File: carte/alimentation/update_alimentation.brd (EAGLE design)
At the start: 160 x 100 mm, 81 parts, among them IC1 LM2596T, IC2 LM2596T, IC4 DSPIC33FJ128MC804PT, J4 RJ11-2L-B, K2 RP811005, U2 LP2985-33DBVR, X10 22-23-2021, X11 22-23-2021, X9 22-23-2021

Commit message: LM2678S_ADJ dimmensionnement
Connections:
- removed net N$25 (its old number): C22.2
- removed net N$29: C20.1, C20.2
- new net N$24: C16.1
- net GND: now also C18.2, C21.2, D3.A, LM2678T-12.4; no longer C16.1
- net N$21: now also C16.2, C22.2; no longer C21.2
- net N$26: now also C19.2, C20.2; no longer C16.2, C18.2, D3.A, LM2678T-12.4
- net N$28: now also C20.1; no longer C19.2
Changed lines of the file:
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@@
 <?xml version="1.0" encoding="utf-8"?>
 <!DOCTYPE eagle SYSTEM "eagle.dtd">
-<eagle version="8.7.0">
+<eagle version="9.0.0">
 <drawing>
 <settings>
@@
 <contactref element="J3" pad="4"/>
 <contactref element="D2" pad="A"/>
-<contactref element="C5" pad="2"/>
 <contactref element="C2" pad="2"/>
 <contactref element="C6" pad="1"/>
@@
 <contactref element="PAD13" pad="1"/>
 <contactref element="PAD14" pad="1"/>
-<contactref element="C16" pad="1"/>
+<contactref element="LM2678T-12" pad="4"/>
+<contactref element="C5" pad="2"/>
 <contactref element="LM2678T-12" pad="2"/>
-<wire x1="-99.91" y1="-3.81" x2="-120.65" y2="-27.155" width="0" layer="19" extent="1-1"/>
-<wire x1="-84.54" y1="7.62" x2="-99.91" y2="-3.81" width="0" layer="19" extent="1-1"/>
-<wire x1="-79.54" y1="1.82" x2="-84.54" y2="7.62" width="0" layer="19" extent="1-1"/>
+<contactref element="D3" pad="A"/>
+<contactref element="C21" pad="2"/>
+<contactref element="C18" pad="2"/>
+<wire x1="-108.37" y1="-34.29" x2="-118.53" y2="-58.42" width="0" layer="19" extent="1-1"/>
+<wire x1="-118.11" y1="-27.155" x2="-108.37" y2="-34.29" width="0" layer="19" extent="1-1"/>
+<wire x1="-120.65" y1="-27.155" x2="-118.11" y2="-27.155" width="0" layer="19" extent="1-1"/>
+<wire x1="-76.2" y1="-16.51" x2="-108.37" y2="-34.29" width="0" layer="19" extent="1-1"/>
+<wire x1="-79.54" y1="1.82" x2="-76.2" y2="-16.51" width="0" layer="19" extent="1-1"/>
+<wire x1="-84.54" y1="7.62" x2="-79.54" y2="1.82" width="0" layer="19" extent="1-1"/>
 <wire x1="-78.74" y1="13.42" x2="-84.54" y2="7.62" width="0" layer="19" extent="1-1"/>
 <wire x1="-72.94" y1="8.42" x2="-78.74" y2="13.42" width="0" layer="19" extent="1-1"/>
@@
 <contactref element="C21" pad="1"/>
 </signal>
-<signal name="N$21">
-<contactref element="C21" pad="2"/>
-</signal>
 <signal name="N$23">
 <contactref element="IC2" pad="3"/>
@@
 <wire x1="-65.1764" y1="24.13" x2="-68.58" y2="24.13" width="0" layer="19" extent="1-1"/>
 </signal>
-<signal name="N$24">
-<contactref element="C22" pad="1"/>
-</signal>
-<signal name="N$26">
-<contactref element="D3" pad="A"/>
-<contactref element="C18" pad="2"/>
-<contactref element="LM2678T-12" pad="4"/>
-<contactref element="C16" pad="2"/>
-<wire x1="-108.37" y1="-34.29" x2="-118.11" y2="-27.155" width="0" layer="19" extent="1-1"/>
-<wire x1="-98.21" y1="-3.81" x2="-118.11" y2="-27.155" width="0" layer="19" extent="1-1"/>
-<wire x1="-76.2" y1="-16.51" x2="-98.21" y2="-3.81" width="0" layer="19" extent="1-1"/>
-</signal>
-<signal name="N$25">
-<contactref element="C22" pad="2"/>
-</signal>
 <signal name="N$27">
 <contactref element="IC1" pad="3"/>
@@
 <contactref element="L4" pad="2"/>
 </signal>
+<signal name="N$21">
+<contactref element="C22" pad="2"/>
+<contactref element="C16" pad="2"/>
+<wire x1="-98.21" y1="-3.81" x2="-118.53" y2="-62.23" width="0" layer="19" extent="1-1"/>
+</signal>
+<signal name="N$26">
+<contactref element="C19" pad="2"/>
+<contactref element="C20" pad="2"/>
+<wire x1="-118.53" y1="-66.04" x2="-118.53" y2="-69.85" width="0" layer="19" extent="1-1"/>
+</signal>
 <signal name="N$22">
+<contactref element="C22" pad="1"/>
+</signal>
+<signal name="N$24">
+<contactref element="C16" pad="1"/>
+</signal>
+<signal name="N$25">
 <contactref element="C19" pad="1"/>
 </signal>
 <signal name="N$28">
-<contactref element="C19" pad="2"/>
-</signal>
-<signal name="N$29">
-<contactref element="C20" pad="2"/>
 <contactref element="C20" pad="1"/>
-<wire x1="-118.53" y1="-69.85" x2="-120.23" y2="-69.85" width="0" layer="19" extent="1-1"/>
 </signal>
 </signals>

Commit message: carte alim maj sch/brd
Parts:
- removed C3: 1000u, resistor:C0603
- removed D1, D2, D3: 1N5624, diode:DO201-15
- removed K2: RP811005, relay:RT-C/O12A5
- removed L1, L2: (no value), inductor-neosid:SM-L15A
- removed L4: 15uH, inductor-coilcraft:DO3316P
- removed LED2: (no value), eagle-ltspice:LED_1206
- added C23, C24, C25: 100uF, rcl:C1210
- added C26, C30: 10uF, rcl:D/7343-31W
- added C27: 220uF, rcl:D/7343-31W
- added C28, C29: 68uF, rcl:D/7343-31W
- added LED1: RED, led:LED5MM
- added LM2678S_ADJ: (no value), Robot_MT:TO-220-7
- added R7: 4.12k, resistor:R0805
- added R8: 1k, resistor:R0805
- added U$10, U$11: 53uH, Robot_MT:KM-3.0_5V3A
- added U$12: RJ26FX102, Robot_MT:RJ6S
- added U$2, U$3: (no value), Robot_MT:TO220ACS
- added U$4, U$5: (no value), Robot_MT:DO-201AD
- added U$6: T9GV1L14-5, Robot_MT:T9G
- added U$7: BSH108, Robot_MT:SOT23
- added U$8: 22.8uH, Robot_MT:KM-3.0
- added U$9: 14.8uH, Robot_MT:KM-2.1
- C1: value (none) -> 220uF; device resistor:C0603 -> rcl:D/7343-31W
- C16, C19, C20: device resistor:C0603 -> rcl:D/7343-31W
- C17: device resistor:C0603 -> rcl:C0603
- C18, C21: value 180uF -> 68uF; device resistor:C0603 -> rcl:D/7343-31W
- C2, C4: value (none) -> 330uF; device resistor:C0603 -> rcl:D/7343-31W
- C22: value 10uF -> 0.01uF; device resistor:C0603 -> rcl:C0603
- C5: value (none) -> 1000uF; device resistor:C0603 -> rcl:E7,5-16
- R5: value 220 -> 500
- moved X9 245.8 mm to (156.5, 85.1), turned to 90 degrees
- moved C17 240.8 mm to (123.2, 62.2)
- moved C22 237.0 mm to (71.1, 78.7), turned to 90 degrees
- moved LM2678T-12 233.4 mm to (89.3, 96.9)
- moved C13 227.4 mm to (146.1, 77.5)
- moved X12 227.2 mm to (156.0, 65.5), turned to 270 degrees
- moved PAD13 223.8 mm to (142.2, 83.8)
- moved C12 221.3 mm to (143.5, 69.8)
- moved X1 215.9 mm to (156.0, 51.9), turned to 270 degrees
- moved PAD11 214.9 mm to (146.1, 83.8)
- moved PAD6 214.9 mm to (133.3, 88.9)
- moved PAD5 213.6 mm to (138.4, 88.9)
- moved PAD4 211.1 mm to (142.2, 88.9)
- moved C11 208.7 mm to (134.6, 69.8)
- moved Q1 208.6 mm to (141.0, 55.9), turned to 180 degrees
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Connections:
- removed net N$14 (its old number): C18.1, LM2678T-12.6
- removed net N$20: C21.1
- removed net N$21: C16.2, C22.2
- removed net N$22: C22.1
- removed net N$23: IC2.3, IC2.5
- removed net N$24: C16.1
- removed net N$25: C19.1
- removed net N$26: C19.2, C20.2
- removed net N$27: IC1.3, IC1.5
- removed net N$28: C20.1
- removed net RB0: D5.A, K2.A2
- removed net RB1: LED2.C, R5.1
- new net 5V_3A: X10.1, X11.1, X12.2, X9.1
- new net N$15: C16.+, C19.+, C20.+, C26.+, C30.+, C4.+, C5.+, IC2.1, LM2678S_ADJ.2, LM2678T-12.2, R8.1, U$6.K, X1.1
- new net RA7: IC4.13, LED1.K, U$7.1
- new net RA8: IC4.32, R5.1
- new net V+: C18.+, C21.+, C28.+, C29.+, U$9.2
- net +5V: now also C1.+, D5.C, U$11.2, U$6.B1; no longer C2.1, L2.2
- net +5V_3A: now also C27.+, U$10.2; no longer C1.1, L1.2
- net GND: now also C1.-, C16.-, C18.-, C19.-, C2.-, C20.-, C21.-, C23.2, C24.2, C25.2, C26.-, C27.-, C28.-, C29.-, C30.-, C4.-, C5.-, IC1.3, IC1.5, IC2.3, IC2.5, LM2678S_ADJ.4, U$2.A, U$3.A, U$4.A, U$5.A, U$7.2, X15.2; no longer C1.2, C18.2, C2.2, C21.2, C3.1, C5.2, D1.A, D2.A, D3.A, LM2678T-12.2
- net N$1: now also LED1.A, R5.2; no longer X13.1
- net N$11: now also C17.2, LM2678T-12.1, U$3.C, U$9.1; no longer C4.1, IC1.1, X15.2
- net N$12: now also U$10.1, U$4.C; no longer D1.C, L1.1
- net N$13: now also C22.1, LM2678S_ADJ.3; no longer C3.2, C5.1, IC2.1, K2.12, X1.1
- net N$16: now also C22.2, LM2678S_ADJ.1, U$2.C, U$8.1; no longer D5.C, K2.A1
- net N$17: now also C23.1, C24.1, C25.1, U$12.E, U$8.2; no longer C17.2, D3.C, LM2678T-12.1
- net N$18: now also D5.A, U$6.B2, U$7.3; no longer L4.1
- net N$19: now also R7.2, U$12.S; no longer L4.2
- net N$6: now also C2.+, IC1.1, U$6.A, X13.1; no longer C4.2, K2.11
- net N$7: now also LM2678S_ADJ.6, R7.1, R8.2; no longer LED2.A, R5.2
- net N$9: now also U$11.1, U$5.C; no longer D2.C, L2.1

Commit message: MAJ carte alim sch/brd
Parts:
- added R10, R11: 560, resistor:R0805
- added R12: 300, resistor:R0805
- added R13: 820, resistor:R0805
- added R14: 240, resistor:R0805
- added R15, R16: 200, resistor:R0805
- added R17: 1600, resistor:R0805
- added R18: 1100, resistor:R0805
- added R19: 220, resistor:R0805
- added R20: 1300, resistor:R0805
- added R9: 270, resistor:R0805
- moved LED1 104.6 mm to (91.4, 34.3)
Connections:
- net N$6 renamed BAT3+
- removed net N$3: X13.2, X14.1
- removed net N$4: X14.2, X15.1
- new net BAT12_11.1V: J2.4, J3.1, R13.1, X14.2, X15.1
- new net BAT1_3.7V: J3.3, R9.1
- new net BAT1_7.4V: J3.2, R11.1
- new net BAT23_22.2V: J1.4, J2.1, R17.1, X13.2, X14.1
- new net BAT2_14.8V: J2.3, R18.1
- new net BAT2_18.5V: J2.2, R20.1
- new net BAT3_25.9V: J1.3
- new net BAT3_29.6V: J1.2
- new net BAT3_33.3V: J1.1
- new net N$20: R10.2, R9.2
- new net N$21: R11.2, R12.2
- new net N$22: R13.2, R14.2
- new net N$23: R18.2, R19.2
- new net N$24: R15.2, R20.2
- new net N$25: R16.2, R17.2
- net GND: now also R10.1, R12.1, R14.1, R15.1, R16.1, R19.1; no longer J1.4, J2.4
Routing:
- net BAT3+: track 0.00 -> 12.7 mm

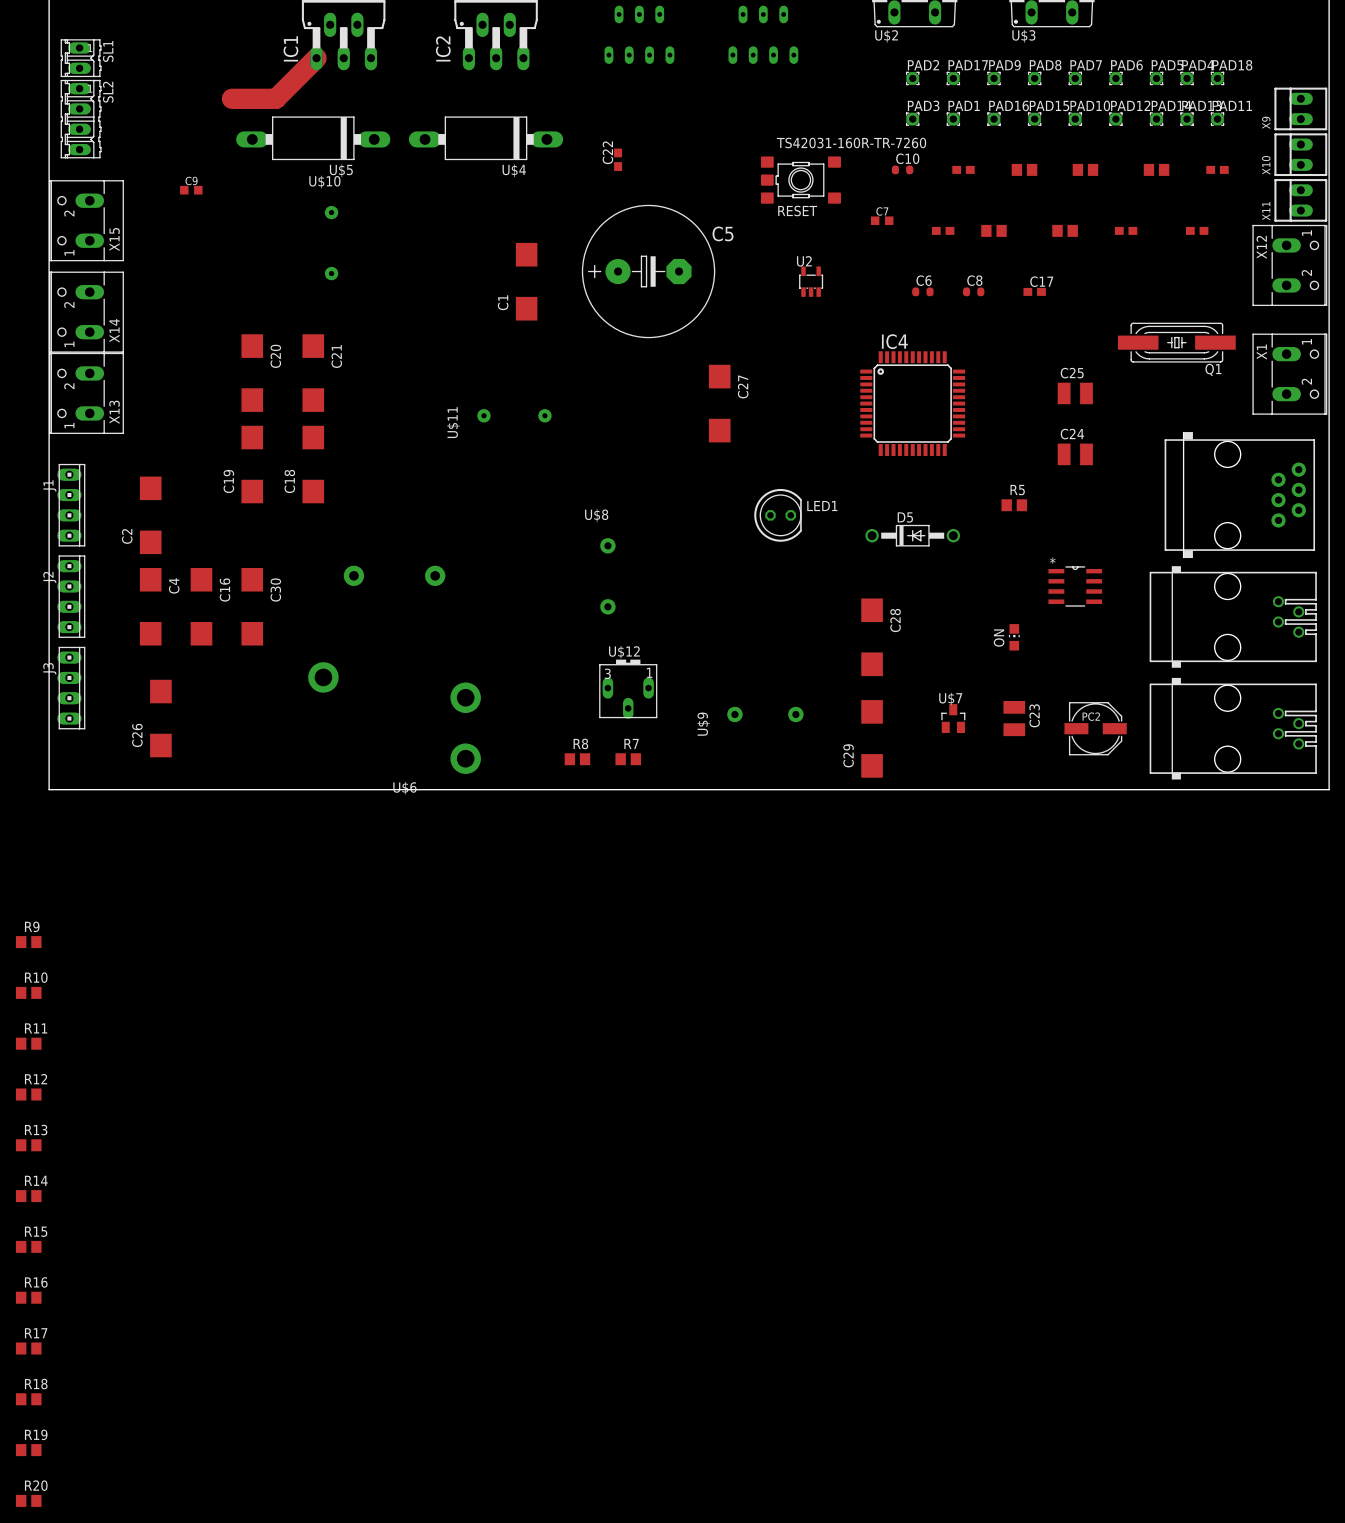
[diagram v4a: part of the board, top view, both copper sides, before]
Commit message: MAJ ancienne carte alim
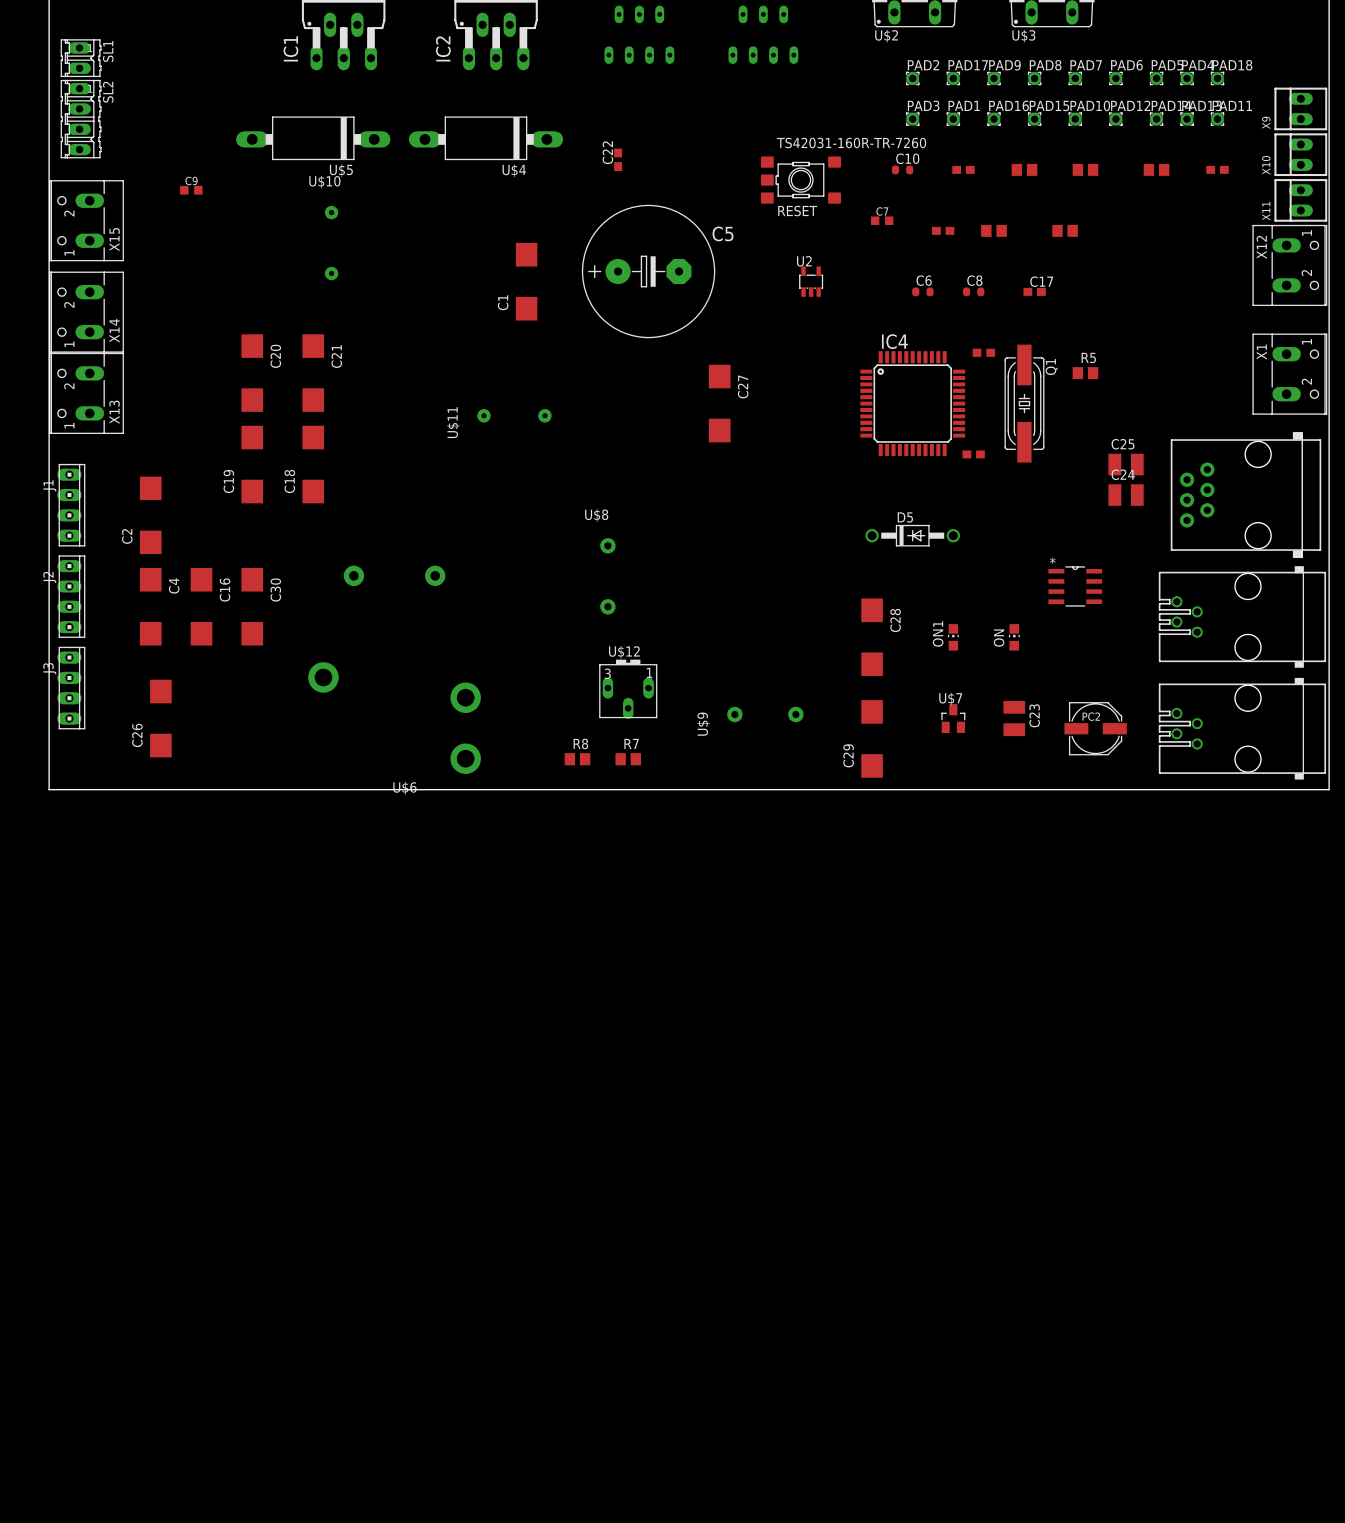
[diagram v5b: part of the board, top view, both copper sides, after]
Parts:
- removed LED1: RED, led:LED5MM
- removed R10, R11: 560, resistor:R0805
- removed R12: 300, resistor:R0805
- removed R13: 820, resistor:R0805
- removed R14: 240, resistor:R0805
- removed R15, R16: 200, resistor:R0805
- removed R17: 1600, resistor:R0805
- removed R18: 1100, resistor:R0805
- removed R19: 220, resistor:R0805
- removed R20: 1300, resistor:R0805
- removed R9: 270, resistor:R0805
- added ON1: GREEN, led:CHIP-LED0805
- moved C12 39.5 mm to (115.6, 41.9)
- moved C11 23.4 mm to (116.8, 54.6)
- moved Q1 20.5 mm to (121.9, 48.3), turned to 270 degrees
- moved R5 18.8 mm to (129.5, 52.1)
- moved C25 10.9 mm to (134.6, 40.6)
- moved C24 8.13 mm to (134.6, 36.8)
- moved J4 3.81 mm to (151.1, 36.8), turned to 90 degrees
- moved J5 2.54 mm to (149.9, 7.62), turned to 90 degrees
- moved J6 2.54 mm to (149.9, 21.6), turned to 90 degrees
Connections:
- net BAT3+ renamed N$6
- removed net BAT12_11.1V: J2.4, J3.1, R13.1, X14.2, X15.1
- removed net BAT1_3.7V: J3.3, R9.1
- removed net BAT1_7.4V: J3.2, R11.1
- removed net BAT23_22.2V: J1.4, J2.1, R17.1, X13.2, X14.1
- removed net BAT2_14.8V: J2.3, R18.1
- removed net BAT2_18.5V: J2.2, R20.1
- removed net BAT3_25.9V: J1.3
- removed net BAT3_29.6V: J1.2
- removed net BAT3_33.3V: J1.1
- removed net N$20: R10.2, R9.2
- removed net N$21: R11.2, R12.2
- removed net N$22: R13.2, R14.2
- removed net N$23: R18.2, R19.2
- removed net N$24: R15.2, R20.2
- removed net N$25: R16.2, R17.2
- new net N$3: X13.2, X14.1
- new net N$4: X14.2, X15.1
- net GND: now also J1.4, J2.4; no longer R10.1, R12.1, R14.1, R15.1, R16.1, R19.1
- net N$1: now also ON1.A; no longer LED1.A
- net RA7: now also ON1.C; no longer LED1.K
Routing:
- net N$6: track 12.7 -> 0.00 mm

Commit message: Modif board + ajout excel
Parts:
- moved U$10 57.2 mm to (36.6, 11.2), turned to 90 degrees
- moved C12 39.5 mm to (143.5, 69.8)
- moved U$11 36.7 mm to (49.3, 11.2)
- moved R7 33.3 mm to (94.0, 29.2)
- moved R8 30.7 mm to (81.3, 30.5)
- moved U$6 30.0 mm to (61.0, 40.6)
- moved C11 23.4 mm to (134.6, 69.8)
- moved Q1 20.5 mm to (141.0, 55.9), turned to 180 degrees
- moved U$12 19.1 mm to (91.4, 14.0)
- moved R5 18.8 mm to (120.7, 35.6)
- moved U$8 17.6 mm to (61.6, 11.2), turned to 90 degrees
- moved U$9 15.6 mm to (74.0, 11.0)
- moved C25 10.9 mm to (128.3, 49.5)
- moved C24 8.13 mm to (128.3, 41.9)
- moved C1 4.02 mm to (55.9, 64.8)
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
